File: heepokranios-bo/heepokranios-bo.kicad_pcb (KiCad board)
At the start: 4 copper layers, 150.1 x 168.4 mm, 242 parts, among them IC1 ADA4945-1ACPZ-R7, IC2 ADA4945-1ACPZ-R7, IC3 ADA4945-1ACPZ-R7, IC4 ADA4945-1ACPZ-R7, IC5 ADA4945-1ACPZ-R7, J1 Conn_02x02_Odd_Even, J11 PGA_13x13, J14 Conn_02x03_Odd_Even, J15 Conn_02x08_Odd_Even, J16 Conn_02x03_Odd_Even, J17 Conn_02x03_Odd_Even, J18 Conn_01x03, J19 Conn_01x03, J2 Conn_02x02_Odd_Even, J20 Conn_01x03, J21 Conn_01x02, J22 Conn_01x03, J23 Conn_02x02_Odd_Even, J24 Conn_02x02_Odd_Even, J25 Conn_02x02_Odd_Even, J26 Conn_01x02, J27 Conn_01x02, J28 Conn_02x02_Odd_Even, J29 Conn_01x02, J3 Conn_02x03_Odd_Even, J30 Conn_01x02, J31 Conn_01x02, J32 Conn_01x02, J33 Conn_01x02, J34 Conn_01x02, J35 Conn_01x02, J36 Conn_01x02, J37 Conn_01x02, J38 Conn_01x02, J39 Conn_01x02, J4 Conn_02x03_Odd_Even, J40 Conn_01x02, J41 Conn_01x02, J42 Conn_01x02, J43 Conn_01x02, J44 Conn_02x02_Odd_Even, J45 Conn_01x03, J48 Conn_01x02, J49 Conn_01x02, J5 Conn_02x03_Odd_Even, J6 Conn_02x04_Odd_Even, J8 Conn_02x03_Odd_Even, J9 Conn_02x02_Odd_Even, SW1 SW_Push, U1 BIWIN_DTS04GE_SMD

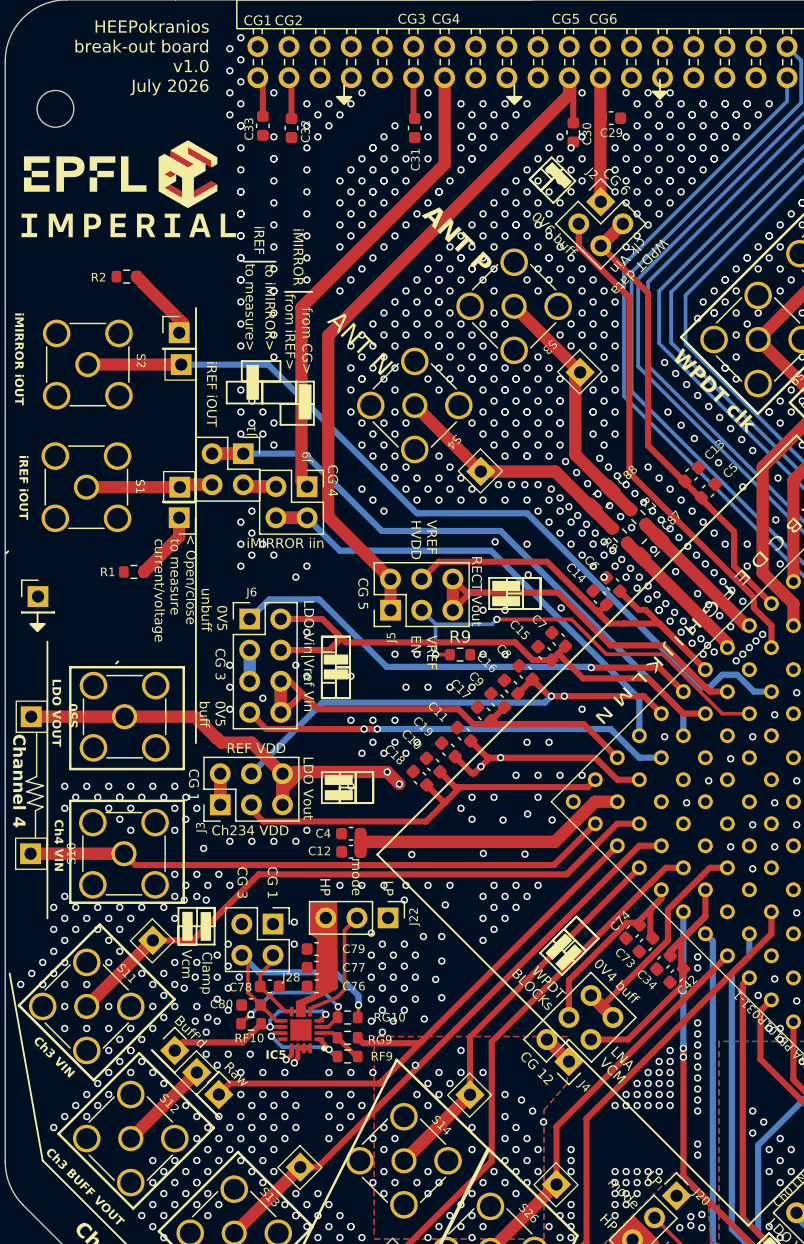
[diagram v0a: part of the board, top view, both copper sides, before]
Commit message: Re-routed with updated PGA 13x13 socket
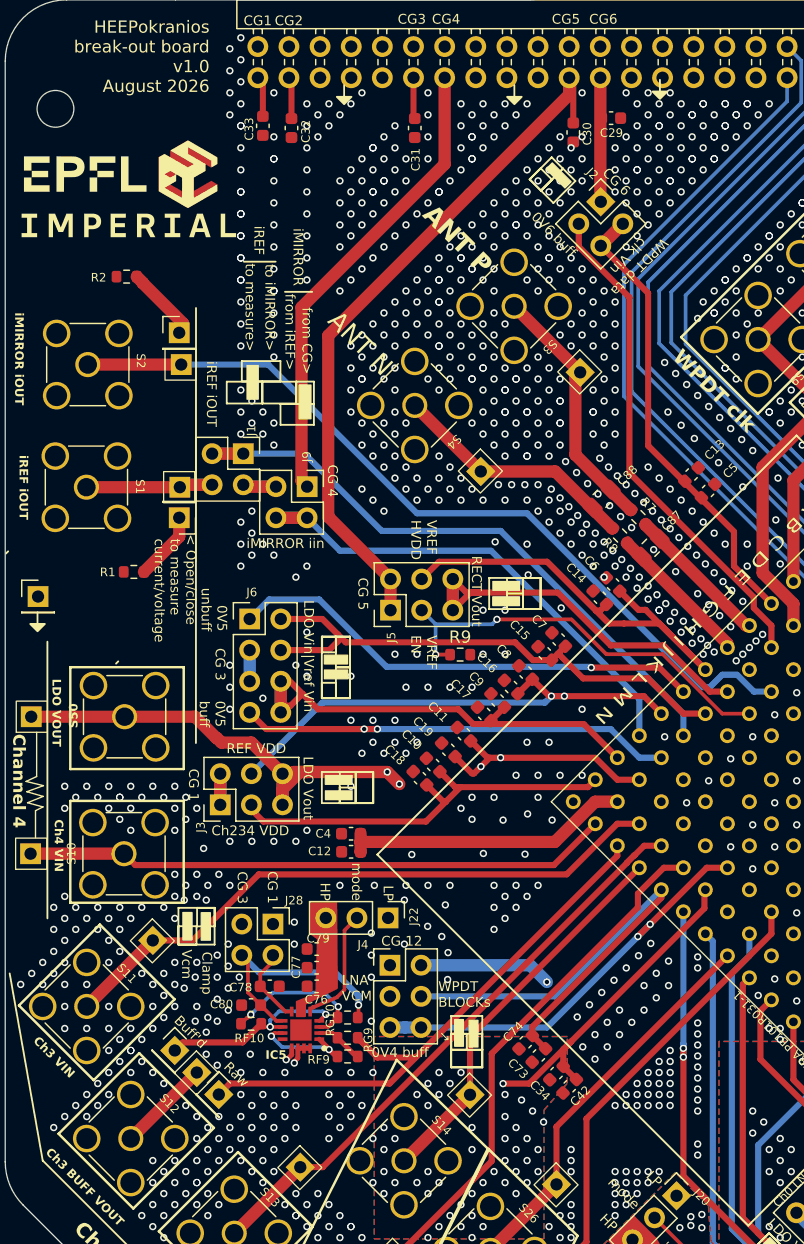
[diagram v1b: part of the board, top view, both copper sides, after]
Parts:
- moved J4 16.6 mm to (54.3, 103.8), turned to 0 degrees
- moved C74 12.6 mm to (65.3, 110.1)
- moved C34 12.6 mm to (67.9, 112.6)
- moved C42 12.6 mm to (68.9, 113.7)
- moved C73 12.6 mm to (66.4, 111.2)
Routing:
- net /WPDT_BLOCKS_VIN: track 17.7 -> 41.0 mm
- net /LNA_VCM_VIN: track 25.4 -> 39.9 mm, vias 0 -> 1
- net /VREF_0V4_BUFF: track 25.0 -> 35.7 mm, vias 0 -> 2
- net /WPDT_LDO_VOUT: track 162.4 -> 159.1 mm
- net /CG_LNA_VCM: track 134.9 -> 133.5 mm, vias 0 -> 1
- net /SE_buffer_2/VIN: track 46.5 -> 47.4 mm
- net GND: vias 3433 -> 3428
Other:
- board text added: "HEEPokranios break-out board v1.0 August 2026"
- board text removed: "HEEPokranios break-out board v1.0 July 2026"
